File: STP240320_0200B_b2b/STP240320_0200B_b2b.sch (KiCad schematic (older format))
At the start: 2 parts, among them J1 Conn_02x08_Odd_Even

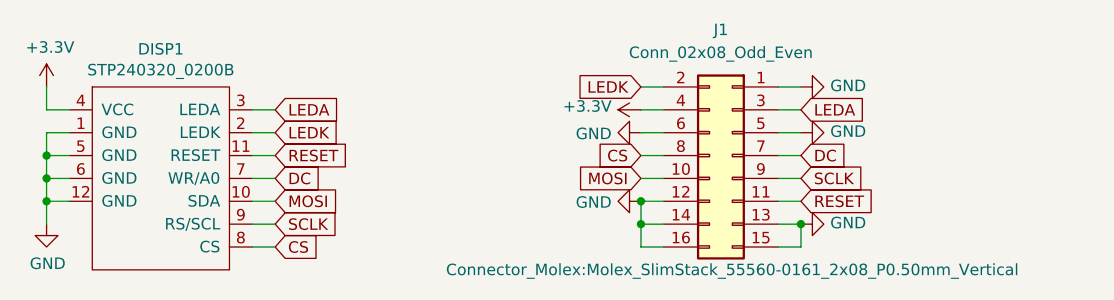
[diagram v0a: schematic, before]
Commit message: Reverse board to board connector pinout.
Display symbol can now be used directly with 54722 parts.
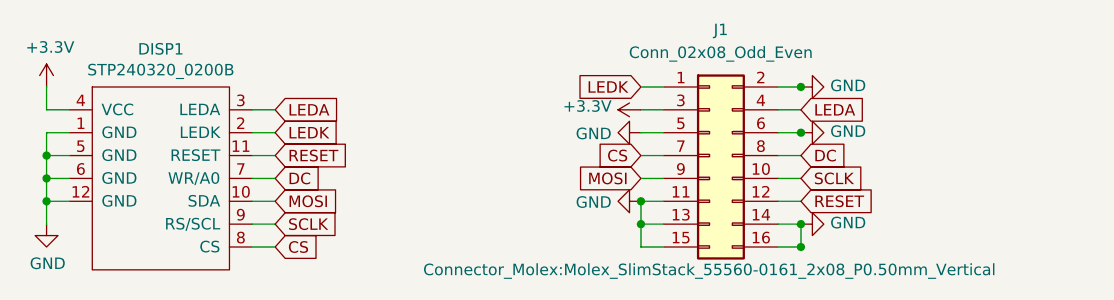
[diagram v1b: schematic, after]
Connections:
- net +3V3: now also J1.3 (Pin_3); no longer J1.4 (Pin_4)
- net CS: now also J1.7 (Pin_7); no longer J1.8 (Pin_8)
- net DC: now also J1.8 (Pin_8); no longer J1.7 (Pin_7)
- net GND: now also J1.11 (Pin_11), J1.2 (Pin_2); no longer J1.1 (Pin_1), J1.12 (Pin_12)
- net LEDA: now also J1.4 (Pin_4); no longer J1.3 (Pin_3)
- net LEDK: now also J1.1 (Pin_1); no longer J1.2 (Pin_2)
- net MOSI: now also J1.9 (Pin_9); no longer J1.10 (Pin_10)
- net RESET: now also J1.12 (Pin_12); no longer J1.11 (Pin_11)
- net SCLK: now also J1.10 (Pin_10); no longer J1.9 (Pin_9)
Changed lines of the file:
@@
 L Connector_Generic:Conn_02x08_Odd_Even J1
 U 1 1 5FC149EE
-P 6800 2300
-F 0 "J1" H 6850 2850 50  0000 C CNN
-F 1 "Conn_02x08_Odd_Even" H 6850 2750 50  0000 C CNN
-F 2 "Connector_Molex:Molex_SlimStack_55560-0161_2x08_P0.50mm_Vertical" H 6800 1800 50  0000 C CNN
-F 3 "~" H 6800 2300 50  0001 C CNN
-	1    6800 2300
-	-1   0    0    -1
+P 6700 2300
+F 0 "J1" H 6750 2850 50  0000 C CNN
+F 1 "Conn_02x08_Odd_Even" H 6750 2750 50  0000 C CNN
+F 2 "Connector_Molex:Molex_SlimStack_55560-0161_2x08_P0.50mm_Vertical" H 6700 1800 50  0000 C CNN
+F 3 "~" H 6700 2300 50  0001 C CNN
+	1    6700 2300
+	1    0    0    -1
 $EndComp
 Wire Wire Line
@@
 Connection ~ 6400 2600
 $Comp
-L power:GND #PWR?
+L power:GND #PWR0101
 U 1 1 5FC2A8B0
 P 7100 2600
-F 0 "#PWR?" H 7100 2350 50  0001 C CNN
+F 0 "#PWR0101" H 7100 2350 50  0001 C CNN
 F 1 "GND" V 7105 2472 50  0000 R CNN
 F 2 "" H 7100 2600 50  0001 C CNN
@@
 	7100 2700 7100 2600
 Connection ~ 7100 2600
+Connection ~ 7100 2700
+Connection ~ 7100 2000
+Connection ~ 7100 2200
 $EndSCHEMATC
